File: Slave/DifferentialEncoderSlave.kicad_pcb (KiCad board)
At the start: 4 copper layers, 52.5 x 24.8 mm, 31 parts, among them J1 Main, J2 Thermistor, J3 Conn_01x06, U1 ADM4852, U2 STM32G4A1KEU4, U3 LP5907MFX-3.3, U4 MA730

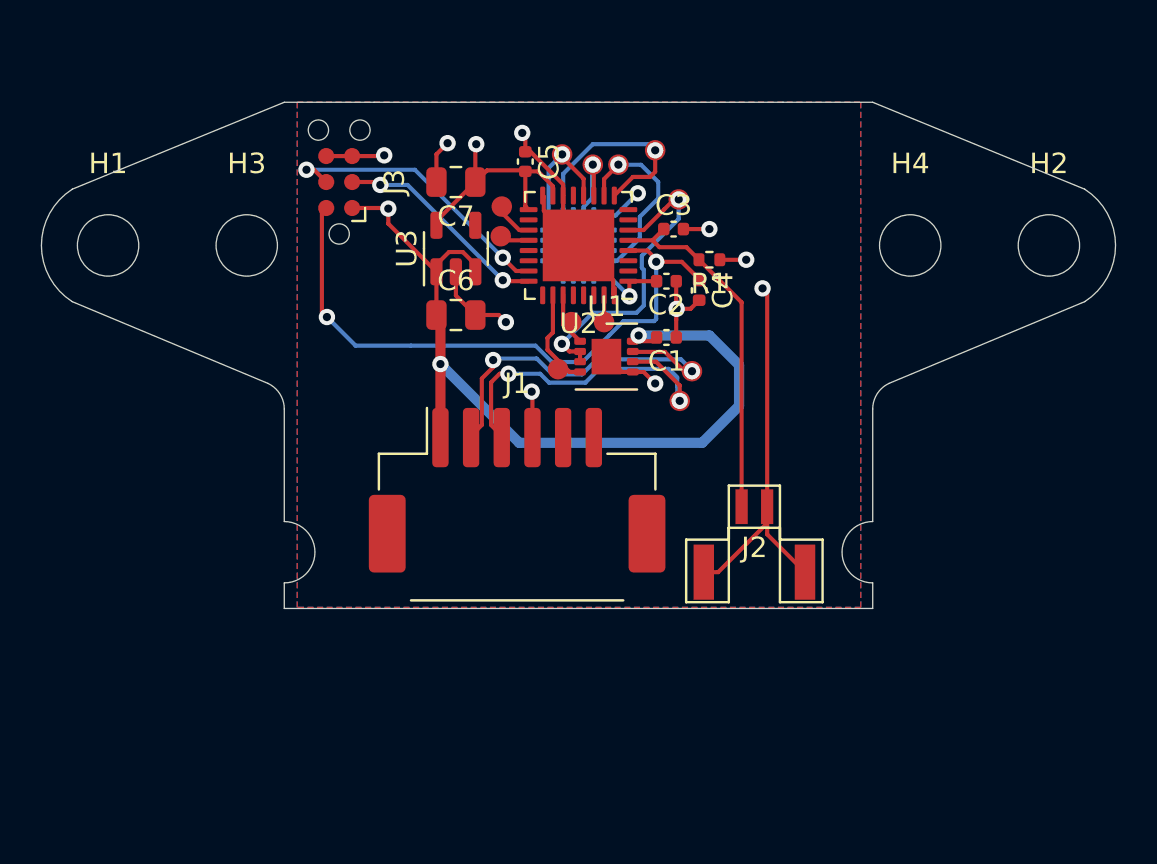
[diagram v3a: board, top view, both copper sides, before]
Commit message: Add RS485 termination resistor
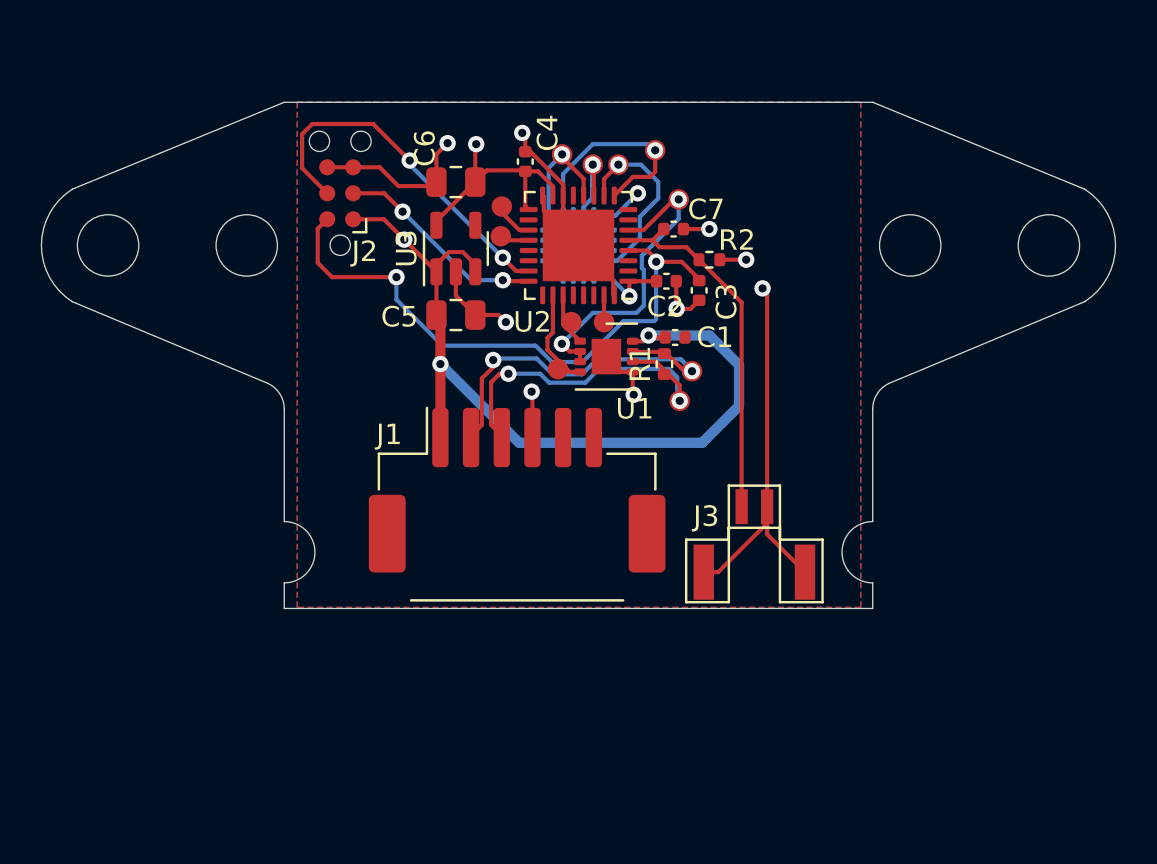
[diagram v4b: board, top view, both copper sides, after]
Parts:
- added R1: 120, Resistor_SMD:R_0402_1005Metric, F.Cu at (126.2, 73.8)
- J2: renamed from J3; value Conn_01x06 -> Debug
- moved J2 0.55 mm to (110.3, 65.5)
- moved C1 0.42 mm to (126.7, 72.5)
- renumbered C4 to C3, C5 to C4, C6 to C5, C7 to C6, C3 to C7, J2 to J3, R1 to R2
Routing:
- net /SWDIO: track 14.1 -> 17.8 mm
- net GNDD: track 59.9 -> 61.3 mm, vias 10 -> 9
- net +5V: track 43.2 -> 42.1 mm
- net /~{RESET}: track 30.3 -> 29.3 mm

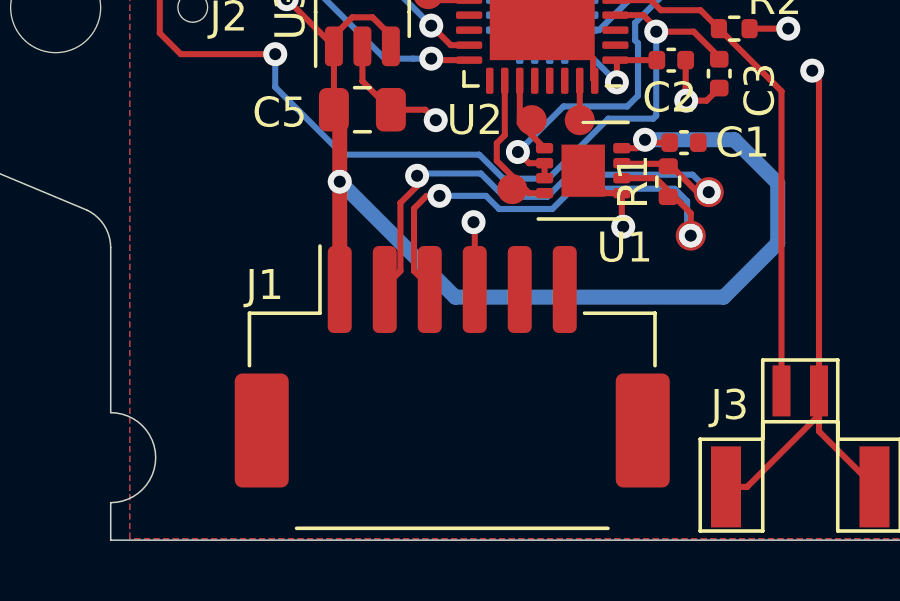
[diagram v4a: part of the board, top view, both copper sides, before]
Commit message: Ground CLIK-Mate shield pins
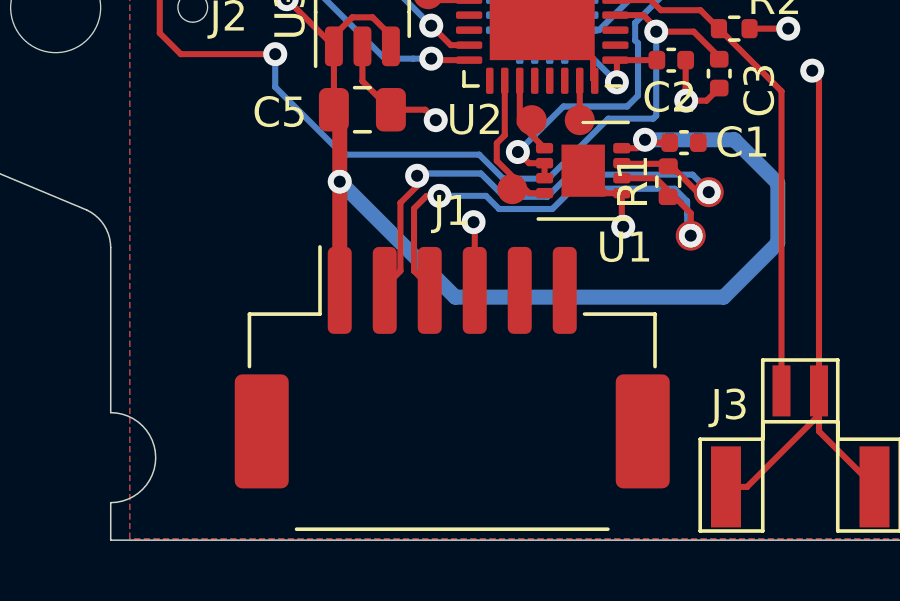
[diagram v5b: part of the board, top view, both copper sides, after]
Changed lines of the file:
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@@
       (net 10 "/BOOT0") (pinfunction "1") (pintype "passive"))
-  )
-  (footprint "Connector_Molex:Molex_CLIK-Mate_502585-0670_1x06-1MP_P1.50mm_Horizontal" (layer "F.Cu")
-    (at 119 79.97)
-    (descr "Molex CLIK-Mate series connector, 502585-0670 (http://www.molex.com/pdm_docs/sd/5025850270_sd.pdf), generated with kicad-footprint-generator")
-    (tags "connector Molex CLIK-Mate top entry")
-    (property "Sheetfile" "DifferentialEncoderSlave.kicad_sch")
-    (property "Sheetname" "")
-    (attr smd)
-    (fp_text reference "J1" (at -6.25 -2.72) (layer "F.SilkS")
-      (effects (font (size 1 1) (thickness 0.15)))
-    )
-    (fp_text value "Main" (at 0 6.48) (layer "F.Fab")
-      (effects (font (size 1 1) (thickness 0.15)))
-    )
-    (fp_text user "${REFERENCE}" (at 0 0.5) (layer "F.Fab")
-      (effects (font (size 1 1) (thickness 0.15)))
-    )
-    (fp_line (start -4.41 -1.785) (end -4.41 -4.025) (layer "F.SilkS") (width 0.12))
-    (fp_line (start -6.76 -1.785) (end -4.41 -1.785) (layer "F.SilkS") (width 0.12))
-    (fp_line (start 6.76 -1.785) (end 4.41 -1.785) (layer "F.SilkS") (width 0.12))
-    (fp_line (start 6.76 -0.035) (end 6.76 -1.785) (layer "F.SilkS") (width 0.12))
-    (fp_line (start -5.19 5.385) (end 5.19 5.385) (layer "F.SilkS") (width 0.12))
-    (fp_line (start -6.76 -0.035) (end -6.76 -1.785) (layer "F.SilkS") (width 0.12))
-    (fp_line (start -7.75 -4.52) (end -7.75 5.78) (layer "F.CrtYd") (width 0.05))
-    (fp_line (start 7.75 -4.52) (end -7.75 -4.52) (layer "F.CrtYd") (width 0.05))
-    (fp_line (start -7.75 5.78) (end 7.75 5.78) (layer "F.CrtYd") (width 0.05))
-    (fp_line (start 7.75 5.78) (end 7.75 -4.52) (layer "F.CrtYd") (width 0.05))
-    (fp_line (start 6.65 -1.675) (end 6.65 2.675) (layer "F.Fab") (width 0.1))
-    (fp_line (start -4.25 -1.675) (end -3.75 -0.967893) (layer "F.Fab") (width 0.1))
-    (fp_line (start -6.65 2.675) (end -6.32 2.675) (layer "F.Fab") (width 0.1))
-    (fp_line (start -3.75 -0.967893) (end -3.25 -1.675) (layer "F.Fab") (width 0.1))
-    (fp_line (start -6.65 -1.675) (end -6.65 2.675) (layer "F.Fab") (width 0.1))
-    (fp_line (start -6.32 2.675) (end -6.32 5.275) (layer "F.Fab") (width 0.1))
-    (fp_line (start 6.32 5.275) (end 6.32 2.675) (layer "F.Fab") (width 0.1))
-    (fp_line (start -6.32 5.275) (end 6.32 5.275) (layer "F.Fab") (width 0.1))
-    (fp_line (start 6.32 2.675) (end 6.65 2.675) (layer "F.Fab") (width 0.1))
-    (fp_line (start -6.65 -1.675) (end 6.65 -1.675) (layer "F.Fab") (width 0.1))
-    (pad "1" smd roundrect (at -3.75 -2.575) (size 0.8 2.9) (layers "F.Cu" "F.Paste" "F.Mask") (roundrect_rratio 0.25)
-      (net 1 "+5V") (pinfunction "Pin_1") (pintype "passive"))
-    (pad "2" smd roundrect (at -2.25 -2.575) (size 0.8 2.9) (layers "F.Cu" "F.Paste" "F.Mask") (roundrect_rratio 0.25)
-      (net 8 "/RS485_N") (pinfunction "Pin_2") (pintype "passive"))
-    (pad "3" smd roundrect (at -0.75 -2.575) (size 0.8 2.9) (layers "F.Cu" "F.Paste" "F.Mask") (roundrect_rratio 0.25)
-      (net 9 "/RS485_P") (pinfunction "Pin_3") (pintype "passive"))
-    (pad "4" smd roundrect (at 0.75 -2.575) (size 0.8 2.9) (layers "F.Cu" "F.Paste" "F.Mask") (roundrect_rratio 0.25)
-      (net 2 "GNDD") (pinfunction "Pin_4") (pintype "passive"))
-    (pad "5" smd roundrect (at 2.25 -2.575) (size 0.8 2.9) (layers "F.Cu" "F.Paste" "F.Mask") (roundrect_rratio 0.25)
-      (net 32 "unconnected-(J1-Pad5)") (pinfunction "Pin_5") (pintype "passive+no_connect"))
-    (pad "6" smd roundrect (at 3.75 -2.575) (size 0.8 2.9) (layers "F.Cu" "F.Paste" "F.Mask") (roundrect_rratio 0.25)
-      (net 34 "unconnected-(J1-Pad6)") (pinfunction "Pin_6") (pintype "passive+no_connect"))
-    (pad "MP" smd roundrect (at 6.35 2.125) (size 1.8 3.8) (layers "F.Cu" "F.Paste" "F.Mask") (roundrect_rratio 0.138889))
-    (pad "MP" smd roundrect (at -6.35 2.125) (size 1.8 3.8) (layers "F.Cu" "F.Paste" "F.Mask") (roundrect_rratio 0.138889))
-    (model "${KIPRJMOD}/3dmodels/5025850670.stp"
-      (offset (xyz 0 -2 3.75))
-      (scale (xyz 1 1 1))
-      (rotate (xyz -90 0 180))
-    )
   )
   (footprint "Resistor_SMD:R_0402_1005Metric" (layer "F.Cu")
@@
       (offset (xyz 0 0 0))
       (scale (xyz 1 1 1))
+      (rotate (xyz 0 0 0))
+    )
+  )
+  (footprint "Connector_Molex:Molex_CLIK-Mate_502585-0670_1x06-1MP_P1.50mm_Horizontal" (layer "F.Cu")
+    (at 119 80)
+    (descr "Molex CLIK-Mate series connector, 502585-0670 (http://www.molex.com/pdm_docs/sd/5025850270_sd.pdf), generated with kicad-footprint-generator")
+    (tags "connector Molex CLIK-Mate top entry")
+    (property "Sheetfile" "DifferentialEncoderSlave.kicad_sch")
+    (property "Sheetname" "")
+    (attr smd)
+    (fp_text reference "J1" (at 0 -5.22) (layer "F.SilkS")
+      (effects (font (size 1 1) (thickness 0.15)))
+    )
+    (fp_text value "Main" (at 0 6.48) (layer "F.Fab")
+      (effects (font (size 1 1) (thickness 0.15)))
+    )
+    (fp_text user "${REFERENCE}" (at 0 0.5) (layer "F.Fab")
+      (effects (font (size 1 1) (thickness 0.15)))
+    )
+    (fp_line (start -5.19 5.385) (end 5.19 5.385) (layer "F.SilkS") (width 0.12))
+    (fp_line (start 6.76 -0.035) (end 6.76 -1.785) (layer "F.SilkS") (width 0.12))
+    (fp_line (start -6.76 -0.035) (end -6.76 -1.785) (layer "F.SilkS") (width 0.12))
+    (fp_line (start 6.76 -1.785) (end 4.41 -1.785) (layer "F.SilkS") (width 0.12))
+    (fp_line (start -4.41 -1.785) (end -4.41 -4.025) (layer "F.SilkS") (width 0.12))
+    (fp_line (start -6.76 -1.785) (end -4.41 -1.785) (layer "F.SilkS") (width 0.12))
+    (fp_line (start 7.75 -4.52) (end -7.75 -4.52) (layer "F.CrtYd") (width 0.05))
+    (fp_line (start -7.75 5.78) (end 7.75 5.78) (layer "F.CrtYd") (width 0.05))
+    (fp_line (start 7.75 5.78) (end 7.75 -4.52) (layer "F.CrtYd") (width 0.05))
+    (fp_line (start -7.75 -4.52) (end -7.75 5.78) (layer "F.CrtYd") (width 0.05))
+    (fp_line (start -6.65 -1.675) (end 6.65 -1.675) (layer "F.Fab") (width 0.1))
+    (fp_line (start -6.65 2.675) (end -6.32 2.675) (layer "F.Fab") (width 0.1))
+    (fp_line (start -4.25 -1.675) (end -3.75 -0.967893) (layer "F.Fab") (width 0.1))
+    (fp_line (start 6.65 -1.675) (end 6.65 2.675) (layer "F.Fab") (width 0.1))
+    (fp_line (start 6.32 5.275) (end 6.32 2.675) (layer "F.Fab") (width 0.1))
+    (fp_line (start -6.32 2.675) (end -6.32 5.275) (layer "F.Fab") (width 0.1))
+    (fp_line (start -6.65 -1.675) (end -6.65 2.675) (layer "F.Fab") (width 0.1))
+    (fp_line (start 6.32 2.675) (end 6.65 2.675) (layer "F.Fab") (width 0.1))
+    (fp_line (start -3.75 -0.967893) (end -3.25 -1.675) (layer "F.Fab") (width 0.1))
+    (fp_line (start -6.32 5.275) (end 6.32 5.275) (layer "F.Fab") (width 0.1))
+    (pad "1" smd roundrect (at -3.75 -2.575) (size 0.8 2.9) (layers "F.Cu" "F.Paste" "F.Mask") (roundrect_rratio 0.25)
+      (net 1 "+5V") (pinfunction "Pin_1") (pintype "passive"))
+    (pad "2" smd roundrect (at -2.25 -2.575) (size 0.8 2.9) (layers "F.Cu" "F.Paste" "F.Mask") (roundrect_rratio 0.25)
+      (net 8 "/RS485_N") (pinfunction "Pin_2") (pintype "passive"))
+    (pad "3" smd roundrect (at -0.75 -2.575) (size 0.8 2.9) (layers "F.Cu" "F.Paste" "F.Mask") (roundrect_rratio 0.25)
+      (net 9 "/RS485_P") (pinfunction "Pin_3") (pintype "passive"))
+    (pad "4" smd roundrect (at 0.75 -2.575) (size 0.8 2.9) (layers "F.Cu" "F.Paste" "F.Mask") (roundrect_rratio 0.25)
+      (net 2 "GNDD") (pinfunction "Pin_4") (pintype "passive"))
+    (pad "5" smd roundrect (at 2.25 -2.575) (size 0.8 2.9) (layers "F.Cu" "F.Paste" "F.Mask") (roundrect_rratio 0.25)
+      (net 32 "unconnected-(J1-Pad5)") (pinfunction "Pin_5") (pintype "passive+no_connect"))
+    (pad "6" smd roundrect (at 3.75 -2.575) (size 0.8 2.9) (layers "F.Cu" "F.Paste" "F.Mask") (roundrect_rratio 0.25)
+      (net 34 "unconnected-(J1-Pad6)") (pinfunction "Pin_6") (pintype "passive+no_connect"))
+    (pad "SH" smd roundrect (at -6.35 2.125) (size 1.8 3.8) (layers "F.Cu" "F.Paste" "F.Mask") (roundrect_rratio 0.138889)
+      (net 2 "GNDD") (pinfunction "Shield") (pintype "passive"))
+    (pad "SH" smd roundrect (at 6.35 2.125) (size 1.8 3.8) (layers "F.Cu" "F.Paste" "F.Mask") (roundrect_rratio 0.138889)
+      (net 2 "GNDD") (pinfunction "Shield") (pintype "passive"))
+    (model "${KICAD6_3DMODEL_DIR}/Connector_Molex.3dshapes/Molex_CLIK-Mate_502585-0670_1x06-1MP_P1.50mm_Horizontal.wrl"
+      (offset (xyz 0 0 0))
+      (scale (xyz 1 1 1))
